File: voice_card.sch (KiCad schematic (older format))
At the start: 44 parts

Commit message: VCO1 and VCO2 done in schematic. Need to check
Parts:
- added C? (x4): 100p, symbol C_US
- added C?: 18p, symbol C_US
- added C?: 2.2n 1%, symbol C_US
- added D?: BAV70, symbol BAV70
- added Q?: BCM847, symbol BCM847
- added Q?: MMBF4391LT1G, symbol MMBF4391LT1G
- added R?: 33K, symbol R_US
- added R? (x6): 56K, symbol R_US
- added R? (x3): 15K, symbol R_US
- added R?: 39K, symbol R_US
- added R? (x2): 1M, symbol R_US
- added R? (x4): 10K, symbol R_US
- added R?: 20K, symbol R_US
- added R?: 3.3K, symbol R_US
- added R?: 680, symbol R_US
- added R?: 1.5M, symbol R_US
- added R?: 91K, symbol R_US
- added TC?: 1K 3300ppm/K, symbol R_US
- added TP?: TEST_POINT, symbol TEST_POINT
- added U?: LF351, symbol CA3140
- added U?: LM311M, symbol LM311M
- added U? (x4): TL074-, symbol TL074-
- added U? (x2): TL072-, ~, symbol TL072-
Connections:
- net labels added: VCO1_PITCH_CV, VCO1_PULSE, VCO1_PWM_CV, VCO1_SAW, VCO1_SCALE, VCO1_SYNC_IN, VCO1_TRI, VCO1_TRI_SHAPE, VCO2_PITCH_CV, VCO2_PULSE, VCO2_PWM_CV, VCO2_SAW, VCO2_SCALE, VCO2_SYNC_IN, VCO2_TRI, VCO2_TRI_SHAPE
- net labels removed: +VCC, -VCC, 0V, PITCH_1_CV, PITCH_CV, PULSE, PULSE_1, PWM_1_CV, PWM_CV, SAW, SAW_1, SCALE, SCALE_1, SYNC, SYNC_1, TRI, TRI_1, TRI_SHAPE_1
- wire segments 165 -> 229
- no-connect marks 3 -> 6

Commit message: added VCA and VCF to voice card schematic. added .gitignore
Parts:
- removed P?: CONN_12, ~, symbol CONN_12
- added C? (x4): 270pF, MyModules:SM0603-C-JRL, symbol C_US
- added C?: 47pF, MyModules:SM0603-C-JRL, symbol C_US
- added C?: 47pF, MyModules:SOIC16-12-JRL, symbol C_US
- added Q?: BC857BS, MyModules:SOT363-JRL, symbol BCM857BS
- added R? (x6): 560, MyModules:SM0603-R-JRL, symbol R_US
- added R? (x2): 150K, MyModules:SM0603-R-JRL, symbol R_US
- added R? (x7): 68K, MyModules:SM0603-R-JRL, symbol R_US
- added R? (x4): 18K, MyModules:SM0603-R-JRL, symbol R_US
- added R? (x2): 100K, MyModules:SM0603-R-JRL, symbol R_US
- added R? (x3): 1.5K, MyModules:SM0603-R-JRL, symbol R_US
- added R?: 4.7K, MyModules:SM0603-R-JRL, symbol R_US
- added R?: 47K, MyModules:SM0603-R-JRL, symbol R_US
- added R?: 1.5M, MyModules:SM0603-R-JRL, symbol R_US
- added R?: 10K, MyModules:SM0603-R-JRL, symbol R_US
- added R?: 1K 3300 ppm/K, MyModules:SM0805-HAND, symbol R_TEMPCO
- added U? (x6): LM13700, MyModules:SOIC16-12-JRL, symbol LM13700
- added U? (x6): TL072-, MyModules:TSSOP8-JRL, symbol TL072-
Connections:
- net labels added: Iabc, OFFSET, RES_CTRL, VCA_CTRL, VCA_OUT, VCF_CTRL, VCF_IN, VCF_OUT
- wire segments 229 -> 435
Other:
- note added: "1"
- note added: "16"
- note added: "1μ DC blocking cap and \n100K resistor (for 10Vp-p input)\nneeded before VCAinput stage.\nSee Juno 106 and Jupiter 8\nschematics."
- note added: "LM13700 Darlington pair buffers not used"
- note added: "VCA"
- note added: "VCF Exponential converter"
- note added: "VCO1 RAMP"
- note added: "VCO2 RAMP"
- moved on the sheet: C?, D?, Q?, R?, TC?, TP?, U?, U?A, U?B, U?C, U?D

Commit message: 2VCOs, 1VCF, 1VCA, 2EGs now in schematic
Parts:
- added C? (x2): 100p, symbol C_US
- added C? (x2): 100n**, symbol C_US
- added C? (x10): 100n, symbol C_US
- added Q? (x2): 2N3904, ~, symbol NPN
- added Q? (x4): DMMT3904, ~, symbol DMMT3904
- added Q? (x4): DMMT3906, ~, symbol DMMT3906
- added R? (x2): 15K, symbol R_US
- added R? (x4): 82K*, symbol R_US
- added R? (x2): 150K, symbol R_US
- added R? (x8): 47K, symbol R_US
- added R? (x6): 2.2K, symbol R_US
- added R? (x2): 1K, symbol R_US
- added R? (x2): 22K, symbol R_US
- added R? (x2): 33K, symbol R_US
- added R? (x6): 100K, symbol R_US
- added R? (x2): 330K, symbol R_US
- added R? (x6): 10K, symbol R_US
- added R? (x4): 270K, symbol R_US
- added R? (x2): 3.3K**, symbol R_US
- added R? (x4): 4.7K, symbol R_US
- added TP? (x12): TEST_POINT, symbol TEST_POINT
- added U? (x8): TL074-, symbol TL074-
- added U? (x2): CD4052, symbol CD4052
- added U? (x2): NE555, ~, symbol NE555
- added U? (x2): 0 - 10V, ~, symbol ENV10V
- added U? (x2): 10 - 0V, ~, symbol ENV10V
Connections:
- net +12V: now also C?.1, C?.1, C?.1, C?.1, C?.1, R?.1, R?.1, R?.1, R?.1, R?.1, R?.1, R?.2, R?.2, R?.2, R?.2, U?.16 (VDD), U?.16 (VDD), U?.4 (R), U?.4 (R), U?.4 (V+), U?.4 (V+), U?.8 (VCC), U?.8 (VCC)
- net -12V: now also C?.2, C?.2, C?.2, R?.1, R?.1, R?.1, R?.1, R?.2, R?.2, U?.11 (V-), U?.11 (V-)
- net GND: now also C?.1, C?.1, C?.1, C?.2, C?.2, C?.2, C?.2, C?.2, Q?.1, Q?.1, Q?.1, Q?.1 (E), Q?.1 (E), Q?.2, R?.1, R?.1, R?.1, R?.1, R?.1, R?.1, R?.2, R?.2, R?.2, R?.2, U?.1 (GND), U?.1 (GND), U?.11 (X3), U?.11 (X3), U?.12 (+), U?.14 (X1), U?.14 (X1), U?.2 (Y2), U?.2 (Y2), U?.3 (+), U?.3 (+), U?.5 (+), U?.6 (Inh), U?.6 (Inh), U?.7 (VEE), U?.7 (VEE), U?.8 (VSS), U?.8 (VSS)
- net OFFSET renamed VCA_IN
- new net: R?.1, R?.2, U?.2 (-) (x3)
- new net: R?.2, R?.2, U?.3 (+) (x2)
- new net: C?.1, R?.1, U?.14
- new net: C?.2, Q?.6, Q?.6, R?.1, U?.13 (-)
- new net: C?.1, Q?.3 (C), R?.1, U?.10 (A) (x2)
- new net: R?.1, U?.13 (X) (x2)
- new net: R?.2, U?.15 (X2) (x2)
- new net: R?.1, U?.3 (Y) (x2)
- new net: U?.3 (Q), U?.9 (B) (x2)
- new net: R?.1, R?.2, TP?.1 (x4)
- new net: R?.1, R?.2, U?.10 (+)
- new net: R?.1, R?.2, TP?.1, U?.8
- new net: R?.1, R?.2, U?.9 (-)
- new net: C?.1, R?.1, R?.1, R?.2, U?.6 (THR), U?.7
- new net: Q?.4, Q?.4, Q?.5, Q?.5, R?.2
- new net: C?.2, Q?.3, Q?.3, U?.6 (-)
- new net: C?.2, R?.2, U?.2 (TR) (x2)
- new net: R?.1, U?.5 (CV) (x2)
- new net: Q?.2 (B), R?.1, R?.1 (x2)
- new net: Q?.2, R?.2, R?.2, R?.2, TP?.1
- new net: Q?.1, R?.2, R?.2, R?.2, TP?.1 (x3)
- new net: C?.1, R?.1, U?.1
- new net: C?.2, Q?.6, Q?.6, R?.1, U?.2 (-)
- new net: R?.1, R?.2, TP?.1, U?.1
- new net: R?.1, R?.2, U?.3 (+)
- new net: C?.1, R?.1, R?.1, R?.2, U?.1, U?.6 (THR)
- new net: Q?.5, Q?.5, Q?.5, Q?.5, R?.2
- new net: C?.2, Q?.6, Q?.6, U?.2 (-)
- new net EG1_ATTACK_CV: R?.1, R?.1
- new net EG1_DECAY_CV: U?.1 (Y0), U?.1 (Y0)
- new net EG1_ENV_OUT: R?.2, R?.2
- new net EG1_GATE: R?.1, R?.1, R?.2, R?.2
- new net EG1_INV_OUT: R?.2, R?.2, U?.1, U?.1
- new net EG1_RELEASE_CV: U?.4 (Y3), U?.4 (Y3), U?.5 (Y1), U?.5 (Y1)
- new net EG1_SUSTAIN_CV: U?.12 (X0), U?.12 (X0)
- no-connect marks 6 -> 8
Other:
- note added: "**adust R to get \nthreshold of 10V"
- note added: "**match C5 value between\n ADSR modules. 95nF gives\nmin attack of <1.5ms"
- note added: "*\nADJUST R7/R8 with T1/T2 \nto get 20-25 s max A/D/R\n"
- note added: "+5V"
- note added: "0-10V CV"
- note added: "1μ DC blocking cap and \n100K resistor (for 10Vp-p input)\nneeded before VCA input stage.\nVCA offset adjust also needed.\nSee Juno 106 and Jupiter 8\nschematics."
- note added: "VC ADSR"
- note added: "original design by Massimo Ischia\nhttp://digilander.libero.it/ismsynth/vc-adsr-1.2.jpg\nadapted for 0-10V input and 0-10V output"
- note removed: "1μ DC blocking cap and \n100K resistor (for 10Vp-p input)\nneeded before VCAinput stage.\nSee Juno 106 and Jupiter 8\nschematics."
- moved on the sheet: C?, D?, Q?, R?, TC?, TP?, U?, U?A, U?B, U?C, U?D

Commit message: added 2x60 120 pin PCI connector to schematic
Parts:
- added P?: CONN_02X60, symbol CONN_02X60
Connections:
- net +12V: now also P?.25 (P25), P?.49 (P49), P?.71 (P71), P?.93 (P93)
- net -12V: now also P?.29 (P29), P?.53 (P53), P?.75 (P75), P?.97 (P97)
- net EG1_ATTACK_CV: now also P?.77 (P77); no longer R?.1
- net EG1_DECAY_CV: now also P?.79 (P79); no longer U?.1 (Y0)
- net EG1_ENV_OUT: now also P?.89 (P89); no longer R?.2
- net EG1_GATE: now also P?.87 (P87); no longer R?.1, R?.2
- net EG1_INV_OUT: now also P?.91 (P91); no longer R?.2, U?.1
- net EG1_RELEASE_CV: now also P?.83 (P83); no longer U?.4 (Y3), U?.5 (Y1)
- net EG1_SUSTAIN_CV: now also P?.81 (P81); no longer U?.12 (X0)
- net GND: now also Q?.2, U?.12 (+), U?.5 (+), P?.107 (P107), P?.15 (P15), P?.27 (P27), P?.39 (P39), P?.51 (P51), P?.63 (P63), P?.73 (P73), P?.85 (P85), P?.95 (P95); no longer Q?.1, U?.3 (+), U?.3 (+)
- net RES_CTRL: now also P?.59 (P59)
- net VCA_CTRL: now also P?.61 (P61)
- net VCA_IN: now also P?.67 (P67)
- net VCA_OUT: now also P?.69 (P69)
- net VCF_CTRL: now also P?.57 (P57)
- net VCF_IN: now also P?.55 (P55)
- net VCF_OUT: now also P?.65 (P65)
- net VCO1_PITCH_CV: now also P?.13 (P13)
- net VCO1_PULSE: now also P?.23 (P23)
- net VCO1_PWM_CV: now also P?.11 (P11)
- net VCO1_SAW: now also P?.21 (P21)
- net VCO1_SCALE: now also P?.17 (P17)
- net VCO1_SYNC_IN: now also P?.9 (P9)
- net VCO1_TRI: now also P?.19 (P19)
- net VCO1_TRI_SHAPE: now also P?.7 (P7)
- net VCO2_PITCH_CV: now also P?.37 (P37)
- net VCO2_PULSE: now also P?.47 (P47)
- net VCO2_PWM_CV: now also P?.35 (P35)
- net VCO2_SAW: now also P?.45 (P45)
- net VCO2_SCALE: now also P?.41 (P41)
- net VCO2_SYNC_IN: now also P?.33 (P33)
- net VCO2_TRI: now also P?.43 (P43)
- net VCO2_TRI_SHAPE: now also P?.31 (P31)
- net at C?.1, R?.1: now also U?.14; no longer U?.1
- net at C?.2, Q?.6, Q?.6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: now also U?.13 (-); no longer U?.2 (-)
- net at R?.1, R?.2, TP?.1: now also U?.8; no longer U?.1
- net at R?.1, R?.2: now also U?.9 (-); no longer U?.2 (-)
- net at R?.1, R?.2: now also U?.10 (+); no longer U?.3 (+)
- net at C?.1, R?.1, R?.1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: now also U?.7; no longer U?.1
- net at Q?.5, Q?.5, R?.2: now also Q?.4, Q?.4; no longer Q?.5, Q?.5
- net at R?.2, R?.2, R?.2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: now also Q?.2; no longer Q?.1
- new net: C?.2, Q?.3, Q?.3, U?.6 (-)
- new net EG2_ATTACK_CV: P?.99 (P99), R?.1
- new net EG2_DECAY_CV: P?.101 (P101), U?.1 (Y0)
- new net EG2_ENV_OUT: P?.111 (P111), R?.2
- new net EG2_GATE: P?.109 (P109), R?.1, R?.2
- new net EG2_INV_OUT: P?.113 (P113), R?.2, U?.1
- new net EG2_RELEASE_CV: P?.105 (P105), U?.4 (Y3), U?.5 (Y1)
- new net EG2_SUSTAIN_CV: P?.103 (P103), U?.12 (X0)

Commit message: annotated schematic, starting assigning footprints
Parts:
- removed U?: TL074-, symbol TL074-
- added unit 1 of U1
- gave numbers to parts that had none: 213
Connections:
- net +12V: now also U1.4 (V+)
- net -12V: now also U1.11 (V-)
- net GND: now also Q10.2, Q7.2, U14.10 (+), U9.10 (+), U1.3 (+); no longer Q10.1, Q7.1, U14.12 (+), U9.12 (+)
- net at D1.2 (A2), R5.2, R6.1: now also U1.1
- net at R12.2, R17.2, R18.2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: now also U1.2 (-)
- net at C22.1, R60.1: now also U9.8; no longer U9.14
- net at C22.2, Q6.6, R67.1: now also Q7.3, TP7.1, U9.9 (-); no longer Q7.6, U9.13 (-)
- net at R69.1, R70.2: now also U9.12 (+); no longer U9.10 (+)
- net at R63.1, R67.2, TP8.1: now also U9.14; no longer U9.8
- net at R63.2, R66.1: now also U9.13 (-); no longer U9.9 (-)
- net at Q6.4, Q6.5, R60.2: now also Q7.4, Q7.5; no longer Q7.4, Q7.5
- net at C21.2, Q6.3, U9.6 (-): now also Q7.6; no longer Q7.3
- net at R62.2, R64.2, R65.2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: now also Q7.1; no longer Q7.2
- net at C28.1, R86.1: now also U14.8; no longer U14.14
- net at C28.2, Q9.6, R93.1: now also Q10.3, U14.9 (-); no longer Q10.6, U14.13 (-)
- net at R95.1, R96.2: now also U14.12 (+); no longer U14.10 (+)
- net at R89.1, R93.2, TP14.1: now also U14.14; no longer U14.8
- net at R89.2, R92.1: now also U14.13 (-); no longer U14.9 (-)
- net at Q9.4, Q9.5, R86.2: now also Q10.4, Q10.5; no longer Q10.4, Q10.5
- net at C27.2, Q9.3, U14.6 (-): now also Q10.6; no longer Q10.3
- net at R88.2, R90.2, R91.2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: now also Q10.1; no longer Q10.2
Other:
- moved on the sheet: C1, C10, C11, C12, C13, C14, C15, C16, C2, C3, C33, C34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

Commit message: fiddling with PCI card edge module. Not sure it's right yet
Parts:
- removed P1: CONN_02X60, symbol CONN_02X60
- removed U11, U16: 10 - 0V, ~, symbol ENV10V
- removed U12, U17: 0 - 10V, ~, symbol ENV10V
- added J1: PCI_11_49, symbol PCI_11_49
- C1: renamed from C17; footprint (none) -> MyModules:SM0603-C-JRL
- C10: renamed from C5; footprint (none) -> MyModules:SM0603-C-JRL
- C11: renamed from C6; footprint (none) -> MyModules:SM0603-C-JRL
- C12: renamed from C7; footprint (none) -> MyModules:SM0603-C-JRL
- C13: renamed from C8; footprint (none) -> MyModules:SM0603-C-JRL
- C14: renamed from C22; footprint (none) -> MyModules:SM0603-C-JRL
- C15: renamed from C9; footprint (none) -> MyModules:SM0805-HAND
- C16: renamed from C10; footprint (none) -> MyModules:SM0603-C-JRL
- C17: renamed from C11; footprint (none) -> MyModules:SM0603-C-JRL
- C18: renamed from C23; footprint (none) -> MyModules:SM0603-C-JRL
- C19: renamed from C24; footprint (none) -> MyModules:SM0603-C-JRL
- C2: renamed from C18; footprint (none) -> MyModules:SM0603-C-JRL
- C20: renamed from C12; footprint (none) -> MyModules:SM0603-C-JRL
- C21: renamed from C13; footprint (none) -> MyModules:SM0603-C-JRL
- C22: renamed from C25; footprint (none) -> MyModules:SM0603-C-JRL
- C23: renamed from C14; footprint (none) -> MyModules:SM0603-C-JRL
- C24: renamed from C15; footprint (none) -> MyModules:SM0603-C-JRL
- C25: renamed from C16; footprint (none) -> MyModules:SM0603-C-JRL
- C26, C27, C28: footprint (none) -> MyModules:SM0603-C-JRL
- C3: renamed from C1; footprint (none) -> MyModules:SM0805-HAND
- C34: footprint MyModules:SOIC16-12-JRL -> MyModules:SM0603-C-JRL
- C4: renamed from C2; footprint (none) -> MyModules:SM0603-C-JRL
- C5: renamed from C19; footprint (none) -> MyModules:SM0603-C-JRL
- C6: renamed from C3; footprint (none) -> MyModules:SM0603-C-JRL
- C7: renamed from C20; footprint (none) -> MyModules:SM0603-C-JRL
- C8: renamed from C21; footprint (none) -> MyModules:SM0603-C-JRL
- C9: renamed from C4; footprint (none) -> MyModules:SM0603-C-JRL
- D1, D2, Q1: footprint (none) -> MyModules:SOT23-JRL
- Q10, Q9: footprint ~ -> MyModules:SOT363-JRL
- Q2: renamed from Q5; footprint ~ -> MyModules:SOT23-JRL
- Q3: renamed from Q2; footprint (none) -> MyModules:SOT363-JRL
- Q4: renamed from Q6; footprint ~ -> MyModules:SOT363-JRL
- Q5: renamed from Q7; footprint ~ -> MyModules:SOT363-JRL
- Q6: renamed from Q3; footprint (none) -> MyModules:SOT23-JRL
- Q7: renamed from Q4; footprint (none) -> MyModules:SOT363-JRL
- Q8: footprint ~ -> MyModules:SOT23-JRL
- R1: renamed from R45; footprint (none) -> MyModules:SM0603-R-JRL
- R10: renamed from R6; footprint (none) -> MyModules:SM0603-R-JRL
- R11: renamed from R7; footprint (none) -> MyModules:SM0603-R-JRL
- R12: renamed from R49; footprint (none) -> MyModules:SM0603-R-JRL
- R13: renamed from R8; footprint (none) -> MyModules:SM0603-R-JRL
- R14: renamed from R50; footprint (none) -> MyModules:SM0603-R-JRL
- R15: renamed from R9; footprint (none) -> MyModules:SM0603-R-JRL
- R16: renamed from R10; footprint (none) -> MyModules:SM0603-R-JRL
- R17: renamed from R11; footprint (none) -> MyModules:SM0603-R-JRL
- R18: renamed from R12; footprint (none) -> MyModules:SM0603-R-JRL
- R19: renamed from R51; footprint (none) -> MyModules:SM0603-R-JRL
- R2: renamed from R1; footprint (none) -> MyModules:SM0603-R-JRL
- R20: renamed from R13; footprint (none) -> MyModules:SM0603-R-JRL
- R21: renamed from R52; footprint (none) -> MyModules:SM0603-R-JRL
- R22: renamed from R14; footprint (none) -> MyModules:SM0603-R-JRL
- R23: renamed from R15; footprint (none) -> MyModules:SM0603-R-JRL
- R24: renamed from R53; footprint (none) -> MyModules:SM0603-R-JRL
- R25: renamed from R54; footprint (none) -> MyModules:SM0603-R-JRL
- R26: renamed from R16; footprint (none) -> MyModules:SM0603-R-JRL
- R27: renamed from R17; footprint (none) -> MyModules:SM0603-R-JRL
- R28: renamed from R18; footprint (none) -> MyModules:SM0603-R-JRL
- R29: renamed from R19; footprint (none) -> MyModules:SM0603-R-JRL
- R3: renamed from R2; footprint (none) -> MyModules:SM0603-R-JRL
- R30: renamed from R55; footprint (none) -> MyModules:SM0603-R-JRL
- R31: renamed from R56; footprint (none) -> MyModules:SM0603-R-JRL
- R32: renamed from R57; footprint (none) -> MyModules:SM0603-R-JRL
- R33: renamed from R58; footprint (none) -> MyModules:SM0603-R-JRL
- R34: renamed from R59; footprint (none) -> MyModules:SM0603-R-JRL
- R35: renamed from R20; footprint (none) -> MyModules:SM0603-R-JRL
- R36: renamed from R21; footprint (none) -> MyModules:SM0603-R-JRL
- R37: renamed from R60; footprint (none) -> MyModules:SM0603-R-JRL
- R38: renamed from R22; footprint (none) -> MyModules:SM0603-R-JRL
- R39: renamed from R61; footprint (none) -> MyModules:SM0603-R-JRL
- R4: renamed from R3; footprint (none) -> MyModules:SM0603-R-JRL
- R40: renamed from R62; footprint (none) -> MyModules:SM0603-R-JRL
- R41: renamed from R63; footprint (none) -> MyModules:SM0603-R-JRL
- R42: renamed from R64; footprint (none) -> MyModules:SM0603-R-JRL
- R43: renamed from R65; footprint (none) -> MyModules:SM0603-R-JRL
- R44: renamed from R66; footprint (none) -> MyModules:SM0603-R-JRL
- R45: renamed from R67; footprint (none) -> MyModules:SM0603-R-JRL
- R46: renamed from R68; footprint (none) -> MyModules:SM0603-R-JRL
- R47: renamed from R69; footprint (none) -> MyModules:SM0603-R-JRL
- R48: renamed from R23; footprint (none) -> MyModules:SM0603-R-JRL
- R49: renamed from R70; footprint (none) -> MyModules:SM0603-R-JRL
- R5: renamed from R46; footprint (none) -> MyModules:SM0603-R-JRL
- R50: renamed from R24; footprint (none) -> MyModules:SM0603-R-JRL
- R51: renamed from R25; footprint (none) -> MyModules:SM0603-R-JRL
- R52: renamed from R26; footprint (none) -> MyModules:SM0603-R-JRL
- R53: renamed from R27; footprint (none) -> MyModules:SM0603-R-JRL
- R54: renamed from R28; footprint (none) -> MyModules:SM0603-R-JRL
- R55: renamed from R29; footprint (none) -> MyModules:SM0603-R-JRL
- R56: renamed from R30; footprint (none) -> MyModules:SM0603-R-JRL
- R57: renamed from R31; footprint (none) -> MyModules:SM0603-R-JRL
- R58: renamed from R32; footprint (none) -> MyModules:SM0603-R-JRL
- R59: renamed from R33; footprint (none) -> MyModules:SM0603-R-JRL
- R6: renamed from R4; footprint (none) -> MyModules:SM0603-R-JRL
- R60: renamed from R34; footprint (none) -> MyModules:SM0603-R-JRL
- R61: renamed from R71; footprint (none) -> MyModules:SM0603-R-JRL
- R62: renamed from R35; footprint (none) -> MyModules:SM0603-R-JRL
- R63: renamed from R36; footprint (none) -> MyModules:SM0603-R-JRL
- R64: renamed from R37; footprint (none) -> MyModules:SM0603-R-JRL
- R65: renamed from R38; footprint (none) -> MyModules:SM0603-R-JRL
- R66: renamed from R39; footprint (none) -> MyModules:SM0603-R-JRL
- R67: renamed from R40; footprint (none) -> MyModules:SM0603-R-JRL
- R68: renamed from R72; footprint (none) -> MyModules:SM0603-R-JRL
- R69: renamed from R41; footprint (none) -> MyModules:SM0603-R-JRL
- R7: renamed from R47; footprint (none) -> MyModules:SM0603-R-JRL
- R70: renamed from R73; footprint (none) -> MyModules:SM0603-R-JRL
- R71: renamed from R74; footprint (none) -> MyModules:SM0603-R-JRL
- R72: renamed from R75; footprint (none) -> MyModules:SM0603-R-JRL
- R73: renamed from R76; footprint (none) -> MyModules:SM0603-R-JRL
- R74: renamed from R42; footprint (none) -> MyModules:SM0603-R-JRL
- R75: renamed from R43; footprint (none) -> MyModules:SM0603-R-JRL
- R76: renamed from R77; footprint (none) -> MyModules:SM0603-R-JRL
- R77: renamed from R78; footprint (none) -> MyModules:SM0603-R-JRL
- R78: renamed from R79; footprint (none) -> MyModules:SM0603-R-JRL
- R79: renamed from R80; footprint (none) -> MyModules:SM0603-R-JRL
- R8: renamed from R48; footprint (none) -> MyModules:SM0603-R-JRL
- R80: renamed from R44; footprint (none) -> MyModules:SM0603-R-JRL
- R81, R82, R83, R84, R85, R86, R87, R88, R89, R90, R91, R92, R93, R94, R95, R96: footprint (none) -> MyModules:SM0603-R-JRL
- R9: renamed from R5; footprint (none) -> MyModules:SM0603-R-JRL
- TC1, TC2: footprint (none) -> MyModules:SM0805-HAND
- TP1, TP10, TP11, TP12, TP13, TP14, TP9: footprint (none) -> MyModules:TEST_POINT_5000_SERIES
- TP2: renamed from TP3; footprint (none) -> MyModules:TEST_POINT_5000_SERIES
- TP3: renamed from TP4; footprint (none) -> MyModules:TEST_POINT_5000_SERIES
- TP4: renamed from TP5; footprint (none) -> MyModules:TEST_POINT_5000_SERIES
- TP5: renamed from TP6; footprint (none) -> MyModules:TEST_POINT_5000_SERIES
- TP6: renamed from TP7; footprint (none) -> MyModules:TEST_POINT_5000_SERIES
- TP7: renamed from TP8; footprint (none) -> MyModules:TEST_POINT_5000_SERIES
- TP8: renamed from TP2; footprint (none) -> MyModules:TEST_POINT_5000_SERIES
- U1: footprint (none) -> Housings_SSOP:TSSOP-14_4.4x5mm_Pitch0.65mm
- U10: renamed from U7; footprint ~ -> MyModules:TSSOP8-JRL
- U11: renamed from U14; footprint (none) -> Housings_SSOP:TSSOP-14_4.4x5mm_Pitch0.65mm
- U12: renamed from U15; footprint ~ -> MyModules:TSSOP8-JRL
- U13: renamed from U8; footprint (none) -> MyModules:TSSOP8-JRL
- U14: renamed from U18; footprint (none) -> Housings_SSOP:TSSOP-16_4.4x5mm_Pitch0.65mm
- U17: renamed from U21; footprint MyModules:SOIC16-12-JRL -> MyModules:SO16-JRL
- U18: renamed from U22; footprint MyModules:SOIC16-12-JRL -> MyModules:SO16-JRL
- U19: renamed from U23; footprint MyModules:SOIC16-12-JRL -> MyModules:SO16-JRL
- U2: renamed from U9; footprint (none) -> Housings_SSOP:TSSOP-14_4.4x5mm_Pitch0.65mm
- U3: renamed from U10; footprint ~ -> MyModules:TSSOP8-JRL
- U4: renamed from U2; footprint (none) -> SMD DIL:so-8
- U5: renamed from U3; footprint ~ -> MyModules:TSSOP8-JRL
- U6: renamed from U4; footprint (none) -> MyModules:TSSOP8-JRL
- U7: renamed from U13; footprint (none) -> Housings_SSOP:TSSOP-16_4.4x5mm_Pitch0.65mm
- U8: renamed from U5; footprint (none) -> Housings_SSOP:TSSOP-14_4.4x5mm_Pitch0.65mm
- U9: renamed from U6; footprint (none) -> SMD DIL:so-8
- renumbered U19 to U15, U20 to U16, U24 to U20
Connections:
- net +12V: now also J1.A1, J1.A13, J1.A25, J1.A36, J1.A47, J1.B1, J1.B13, J1.B25, J1.B36, J1.B47
- net -12V: now also J1.A15, J1.A27, J1.A3, J1.A38, J1.A49, J1.B15, J1.B27, J1.B3, J1.B38, J1.B49
- net EG1_ATTACK_CV: now also J1.A39, J1.B39
- net EG1_DECAY_CV: now also J1.A40, J1.B40
- net EG1_ENV_OUT: now also J1.A45, J1.B45
- net EG1_GATE: now also J1.A44, J1.B44
- net EG1_INV_OUT: now also J1.A46, J1.B46
- net EG1_RELEASE_CV: now also J1.A42, J1.B42
- net EG1_SUSTAIN_CV: now also J1.A41, J1.B41
- net EG2_ATTACK_CV: now also J1.A50, J1.B50
- net EG2_DECAY_CV: now also J1.A51, J1.B51
- net EG2_ENV_OUT: now also J1.A56, J1.B56
- net EG2_GATE: now also J1.A55, J1.B55
- net EG2_INV_OUT: now also J1.A57, J1.B57
- net EG2_RELEASE_CV: now also J1.A53, J1.B53
- net EG2_SUSTAIN_CV: now also J1.A52, J1.B52
- net GND: now also J1.A14, J1.A2, J1.A20, J1.A26, J1.A32, J1.A37, J1.A43, J1.A48, J1.A54, J1.A58, J1.A59, J1.A60, J1.A8, J1.B14, J1.B2, J1.B20, J1.B26, J1.B32, J1.B37, J1.B43, J1.B48, J1.B54, J1.B58, J1.B59, J1.B60, J1.B8
- net RES_CTRL: now also J1.A30, J1.B30
- net VCA_CTRL: now also J1.A31, J1.B31
- net VCA_IN: now also J1.A34, J1.B34
- net VCA_OUT: now also J1.A35, J1.B35
- net VCF_CTRL: now also J1.A29, J1.B29
- net VCF_IN: now also J1.A28, J1.B28
- net VCF_OUT: now also J1.A33, J1.B33
- net VCO1_PITCH_CV: now also J1.A7, J1.B7
- net VCO1_PULSE: now also J1.A12, J1.B12
- net VCO1_PWM_CV: now also J1.A6, J1.B6
- net VCO1_SAW: now also J1.A11, J1.B11
- net VCO1_SCALE: now also J1.A9, J1.B9
- net VCO1_SYNC_IN: now also J1.A5, J1.B5
- net VCO1_TRI: now also J1.A10, J1.B10
- net VCO1_TRI_SHAPE: now also J1.A4, J1.B4
- net VCO2_PITCH_CV: now also J1.A19, J1.B19
- net VCO2_PULSE: now also J1.A24, J1.B24
- net VCO2_PWM_CV: now also J1.A18, J1.B18
- net VCO2_SAW: now also J1.A23, J1.B23
- net VCO2_SCALE: now also J1.A21, J1.B21
- net VCO2_SYNC_IN: now also J1.A17, J1.B17
- net VCO2_TRI: now also J1.A22, J1.B22
- net VCO2_TRI_SHAPE: now also J1.A16, J1.B16
- net at C28.2, Q10.3, Q9.6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: now also TP13.1

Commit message: laying out and routing VCO1 core
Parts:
- J1: footprint (none) -> MyModules:PCI-49-11-CARD-EDGE
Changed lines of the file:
@@
 F 0 "J1" H 8050 25600 60  0000 C CNN
 F 1 "PCI_11_49" H 8050 19200 60  0000 C CNN
-F 2 "" H 8050 22400 60  0000 C CNN
+F 2 "MyModules:PCI-49-11-CARD-EDGE" H 8050 22400 60  0001 C CNN
 F 3 "" H 8050 22400 60  0000 C CNN
 	1    8050 22400

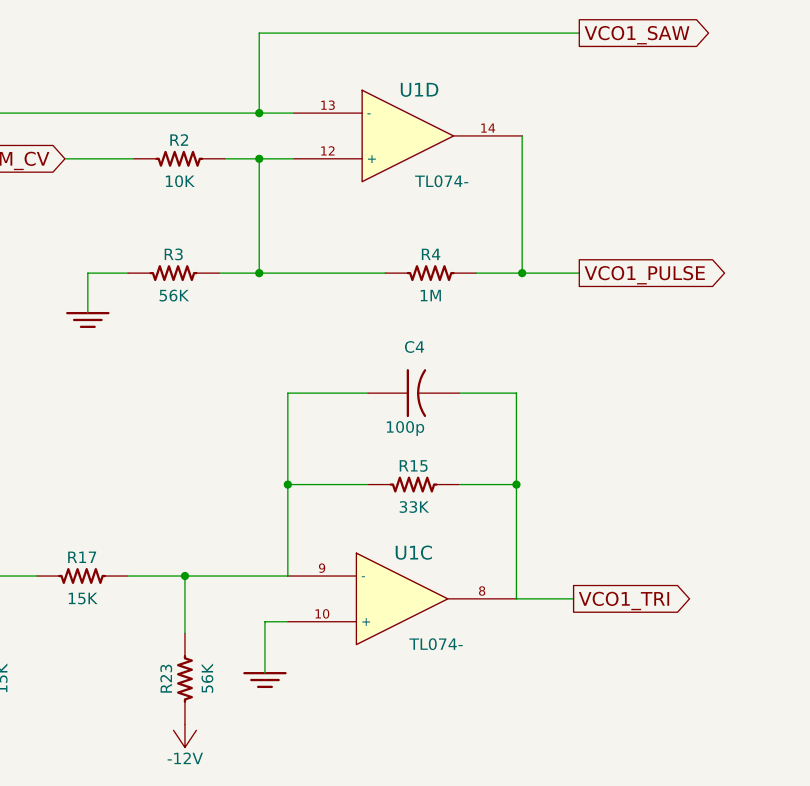
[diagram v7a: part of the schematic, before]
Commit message: starting to layout waveshapers for VCO1
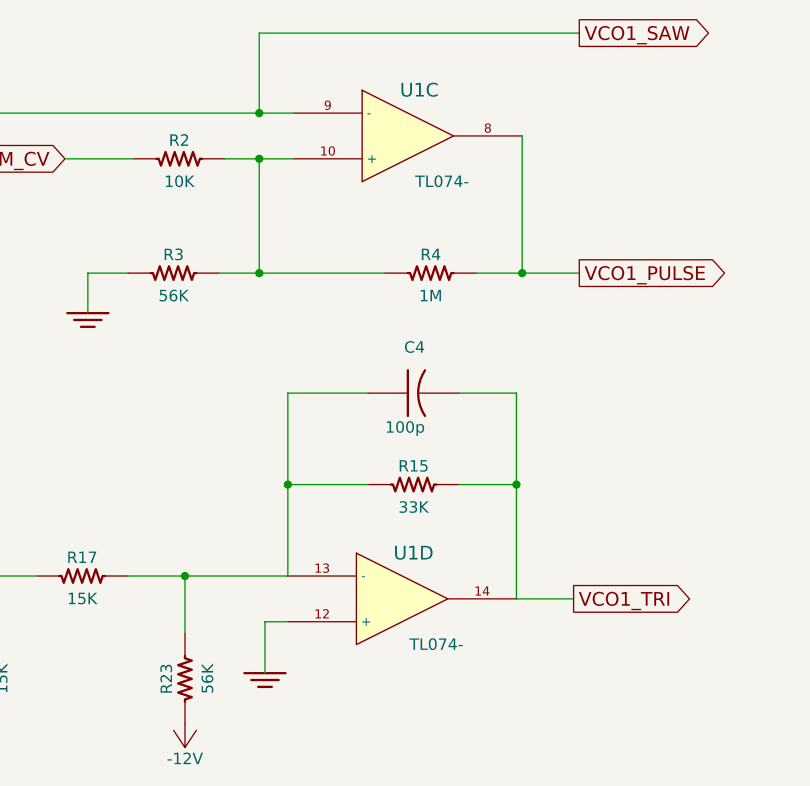
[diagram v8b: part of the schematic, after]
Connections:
- net GND: now also U1.12 (+); no longer U1.10 (+)
- net VCO1_PULSE: now also U1.8; no longer U1.14
- net VCO1_SAW: now also U1.9 (-); no longer U1.13 (-)
- net VCO1_TRI: now also U1.14; no longer U1.8
- net at C4.1, R15.1, R17.2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: now also U1.13 (-); no longer U1.9 (-)
- net at R2.1, R3.1, R4.2: now also U1.10 (+); no longer U1.12 (+)
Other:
- moved on the sheet: U1C, U1D
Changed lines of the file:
@@
 L TL074- U1
 U 4 1 564D0EBB
+P 19625 5375
+F 0 "U1" H 19675 5575 60  0000 C CNN
+F 1 "TL074-" H 19775 5175 50  0000 C CNN
+F 2 "Housings_SSOP:TSSOP-14_4.4x5mm_Pitch0.65mm" H 19625 5375 60  0001 C CNN
+F 3 "" H 19625 5375 60  0000 C CNN
+	4    19625 5375
+	1    0    0    -1
+$EndComp
+$Comp
+L TL074- U1
+U 3 1 564D0EBC
 P 19650 3350
 F 0 "U1" H 19700 3550 60  0000 C CNN
@@
 F 2 "Housings_SSOP:TSSOP-14_4.4x5mm_Pitch0.65mm" H 19650 3350 60  0001 C CNN
 F 3 "" H 19650 3350 60  0000 C CNN
-	4    19650 3350
+	3    19650 3350
 	1    0    0    -1
 $EndComp
-$Comp
-L TL074- U1
-U 3 1 564D0EBC
-P 19625 5375
-F 0 "U1" H 19675 5575 60  0000 C CNN
-F 1 "TL074-" H 19775 5175 50  0000 C CNN
-F 2 "Housings_SSOP:TSSOP-14_4.4x5mm_Pitch0.65mm" H 19625 5375 60  0001 C CNN
-F 3 "" H 19625 5375 60  0000 C CNN
-	3    19625 5375
-	1    0    0    -1
-$EndComp
